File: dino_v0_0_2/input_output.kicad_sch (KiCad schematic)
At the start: 27 parts, among them SW1 SW_DIP_x08

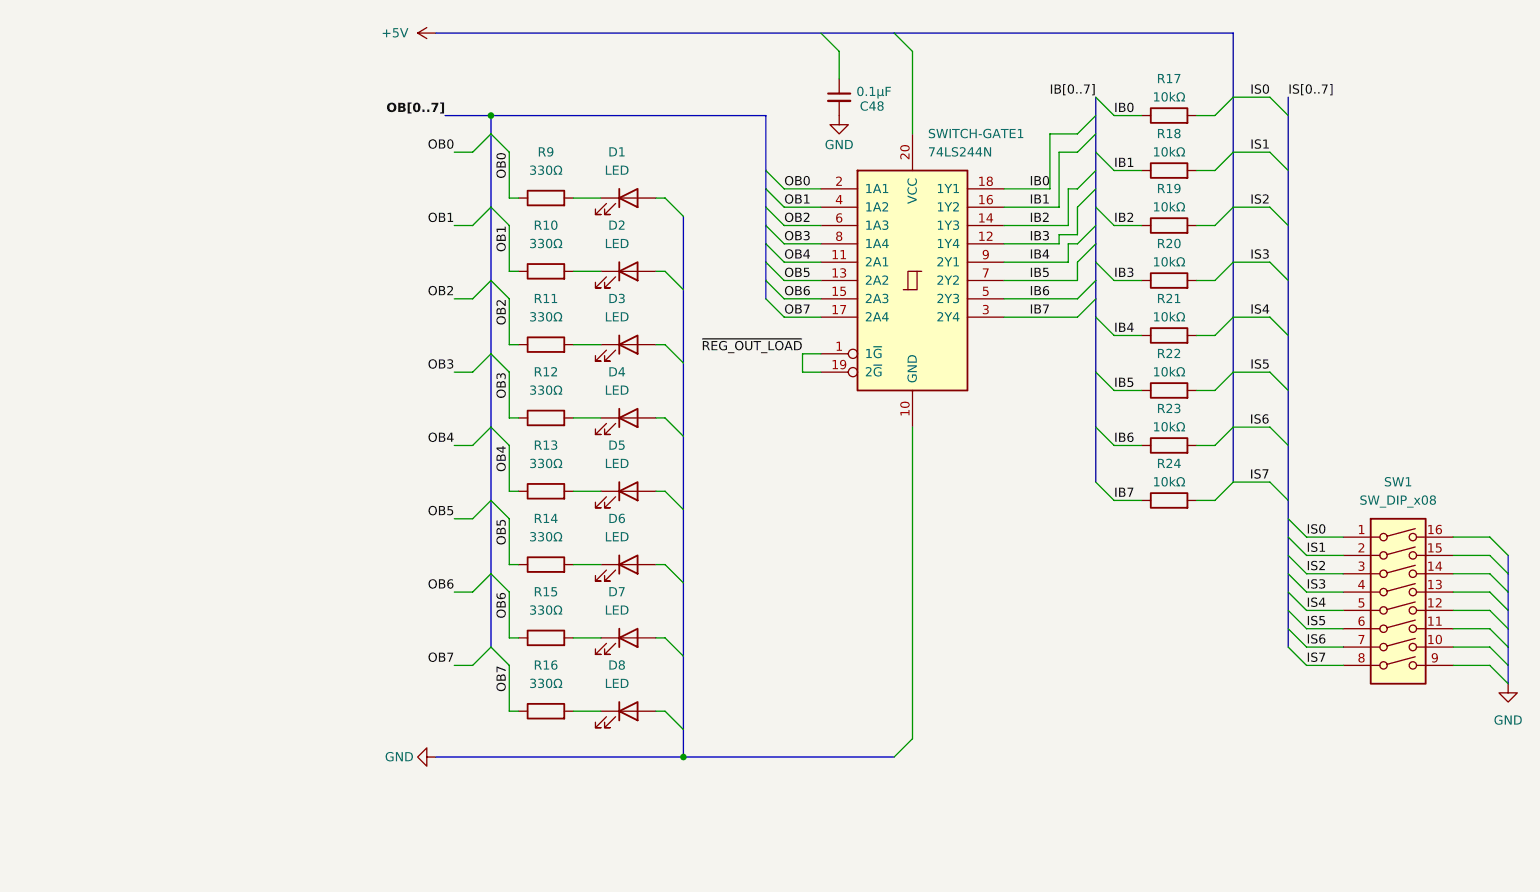
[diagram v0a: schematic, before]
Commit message: feat(dino): complete v0.0.3 schematic — all 11 sheets netlist-clean
- wire MAR sheet: '373 LO/HI latches, 2x '245 M-bus drive, A15 decode
  (ROM_EN/~RAM_EN), LE stamps off /MAR_LO_LOAD//MAR_HI_LOAD
- fix PC_MAR_MUX polarity: PC '245s enabled on bit14=0, inverted vs
  bit-map convention (PC=1); add ~PC_MAR_MUX inverter, relabel U13/U14
- wire all 7 control-word bus taps [15:9] (SA0-2, END, PC_UP,
  PC_MAR_MUX, HALT) — label pairs had no wire between them
- untie NONE/NC '138 outputs: totem-pole bus fight on every microword;
  each unused output now individually no_connect
- build END (U61 NOR: ~MR = RESET|END, sync T-state clear) and HALT
  (T-state freeze via CET, clock keeps running)
- build COND/JNZ (U62: ~PC_LOAD = taken-JNZ | unconditional-JMP)
- claim src code 111 as /SW_OUT: IN port — DIP switches through 10k
  pull-ups onto W bus via '244; LED bank active-high off OB0-7
- add U66 missing power unit + decouplers (C63-C66)
- tools: kicad_gen_sheet.py (declarative YAML/JSON sheet generator,
  deterministic uuid5, collision-checked), kicad_xsheet_audit.py
  (cross-sheet contract audit); archive stale testing-strategy doc
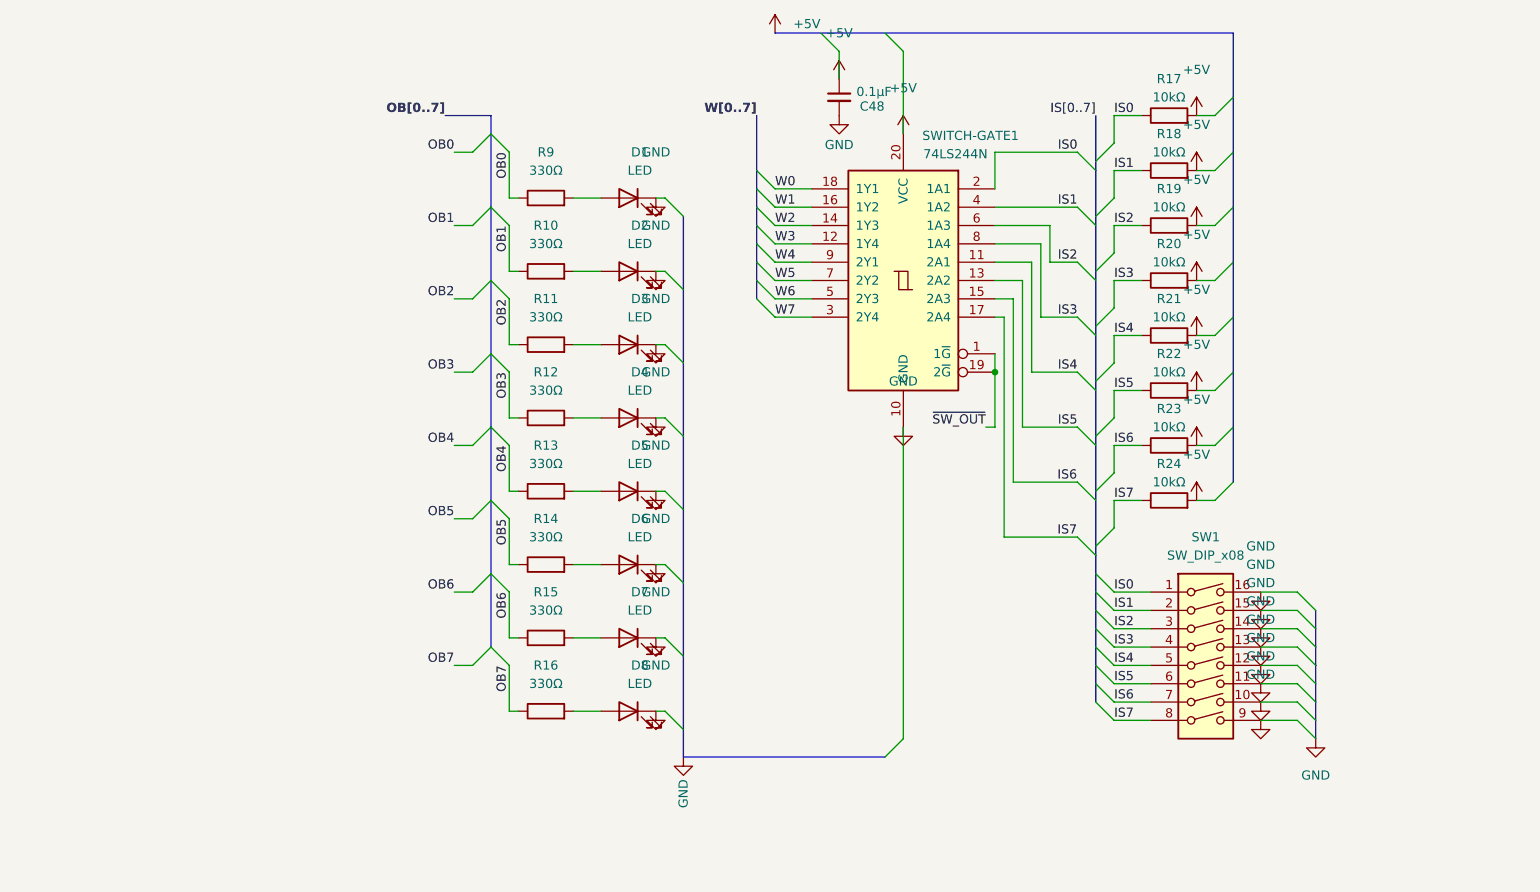
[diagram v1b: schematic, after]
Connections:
- net +5V: now also C48.1, R17.2, R18.2, R19.2, R20.2, R21.2, R22.2, R23.2, R24.2, SWITCH-GATE1.20 (VCC)
- net GND: now also D1.1 (K), D2.1 (K), D3.1 (K), D4.1 (K), D5.1 (K), D6.1 (K), D7.1 (K), D8.1 (K), SW1.10, SW1.11, SW1.12, SW1.13, SW1.14, SW1.15, SW1.16, SW1.9, SWITCH-GATE1.10 (GND)
- net IS0: now also R17.1, SWITCH-GATE1.2 (1A1)
- net IS1: now also R18.1, SWITCH-GATE1.4 (1A2)
- net IS2: now also R19.1, SWITCH-GATE1.6 (1A3)
- net IS3: now also R20.1, SWITCH-GATE1.8 (1A4)
- net IS4: now also R21.1, SWITCH-GATE1.11 (2A1)
- net IS5: now also R22.1, SWITCH-GATE1.13 (2A2)
- net IS6: now also R23.1, SWITCH-GATE1.15 (2A3)
- net IS7: now also R24.1, SWITCH-GATE1.17 (2A4)
- net OB0: no longer SWITCH-GATE1.2 (1A1)
- net OB1: no longer SWITCH-GATE1.4 (1A2)
- net OB2: no longer SWITCH-GATE1.6 (1A3)
- net OB3: no longer SWITCH-GATE1.8 (1A4)
- net OB4: no longer SWITCH-GATE1.11 (2A1)
- net OB5: no longer SWITCH-GATE1.13 (2A2)
- net OB6: no longer SWITCH-GATE1.15 (2A3)
- net OB7: no longer SWITCH-GATE1.17 (2A4)
- net at R14.2: now also D6.2 (A); no longer D6.1 (K)
- net at R10.2: now also D2.2 (A); no longer D2.1 (K)
- net at R13.2: now also D5.2 (A); no longer D5.1 (K)
- net at R12.2: now also D4.2 (A); no longer D4.1 (K)
- net at R9.2: now also D1.2 (A); no longer D1.1 (K)
- net at R11.2: now also D3.2 (A); no longer D3.1 (K)
- net at R15.2: now also D7.2 (A); no longer D7.1 (K)
- net at R16.2: now also D8.2 (A); no longer D8.1 (K)
- net IB0 renamed W0
- net W0: no longer R17.1
- net IB1 renamed W1
- net W1: no longer R18.1
- net IB2 renamed W2
- net W2: no longer R19.1
- net IB3 renamed W3
- net W3: no longer R20.1
- net IB4 renamed W4
- net W4: no longer R21.1
- net IB5 renamed W5
- net W5: no longer R22.1
- net IB6 renamed W6
- net W6: no longer R23.1
- net IB7 renamed W7
- net W7: no longer R24.1
- net ~{REG_OUT_LOAD} renamed ~{SW_OUT}
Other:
- moved on the sheet: D1, D2, D3, D4, D5, D6, D7, D8, SW1, SWITCH-GATE1

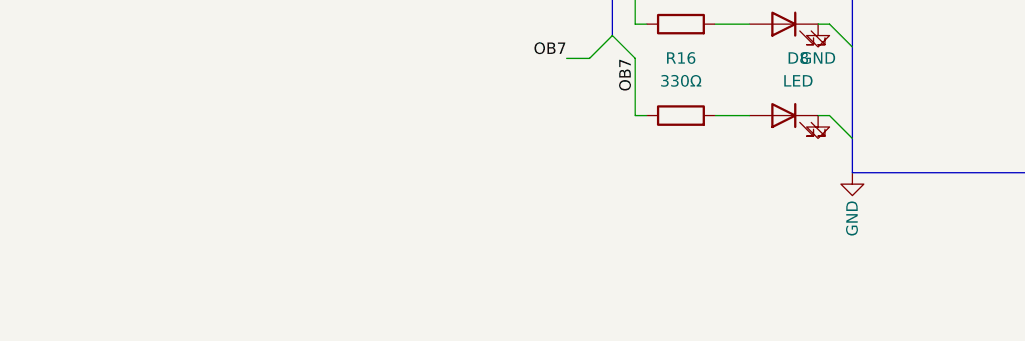
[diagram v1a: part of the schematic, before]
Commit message: feat(dino): generate + stamp per-sheet I/O contracts
Each module's boundary signals (IN/OUT/BIDIR with counterpart sheets)
derived from the kicad-cli netlist and placed as a text block on the
physical sheet, so a bench rig knows exactly what to drive and observe
per board. kicad_contracts.py regenerates both the markdown and the
stamps idempotently; stamping verified electrically neutral.
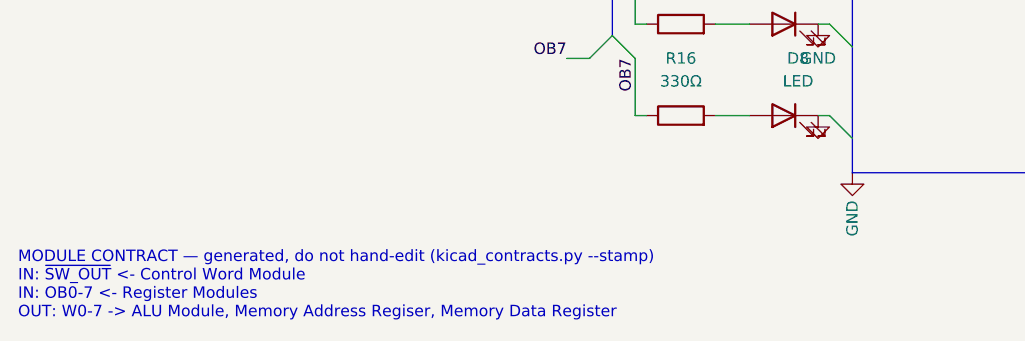
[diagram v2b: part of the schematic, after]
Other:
- note added: "MODULE CONTRACT — generated, do not hand-edit (kicad_contracts.py --stamp) IN: ~{SW_OUT} <- Control Word Module IN: OB0-7 <- Register Modules OUT: W0-7 -> ALU Module, Memory Address Regiser, Memory Data Register"
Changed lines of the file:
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@@
+		)
+	)
+	(text "MODULE CONTRACT — generated, do not hand-edit (kicad_contracts.py --stamp)\nIN: ~{SW_OUT} <- Control Word Module\nIN: OB0-7 <- Register Modules\nOUT: W0-7 -> ALU Module, Memory Address Regiser, Memory Data Register"
+		(exclude_from_sim no)
+		(at 15.24 168.75 0)
+		(effects
+			(font
+				(size 1.27 1.27)
+			)
+			(justify left bottom)
 		)
 	)
